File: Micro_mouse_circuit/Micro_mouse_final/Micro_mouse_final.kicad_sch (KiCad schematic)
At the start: 84 parts, among them J1 Conn_01x02, J2 USB_C_Receptacle_PowerOnly_6P, J3 Conn_02x16_Odd_Even, J4 Conn_01x01_Pin, U1 INA219AxDCN, U10 SN74LVC1G3157DCKR, U11 TPS22917DBVR, U12 AMS1117-3.3, U13 TPS22917DBVR, U14 SK22D15L5, U2 AMS1117-3.3, U3 HUSB237-AA001-DN06R, U4 MT3608, U5 LM2596SX-5_0/NOPB, U6 SK22D15L5, U7 L298N_C19922, U8 L298N_C19922, U9 TP4056_C382139

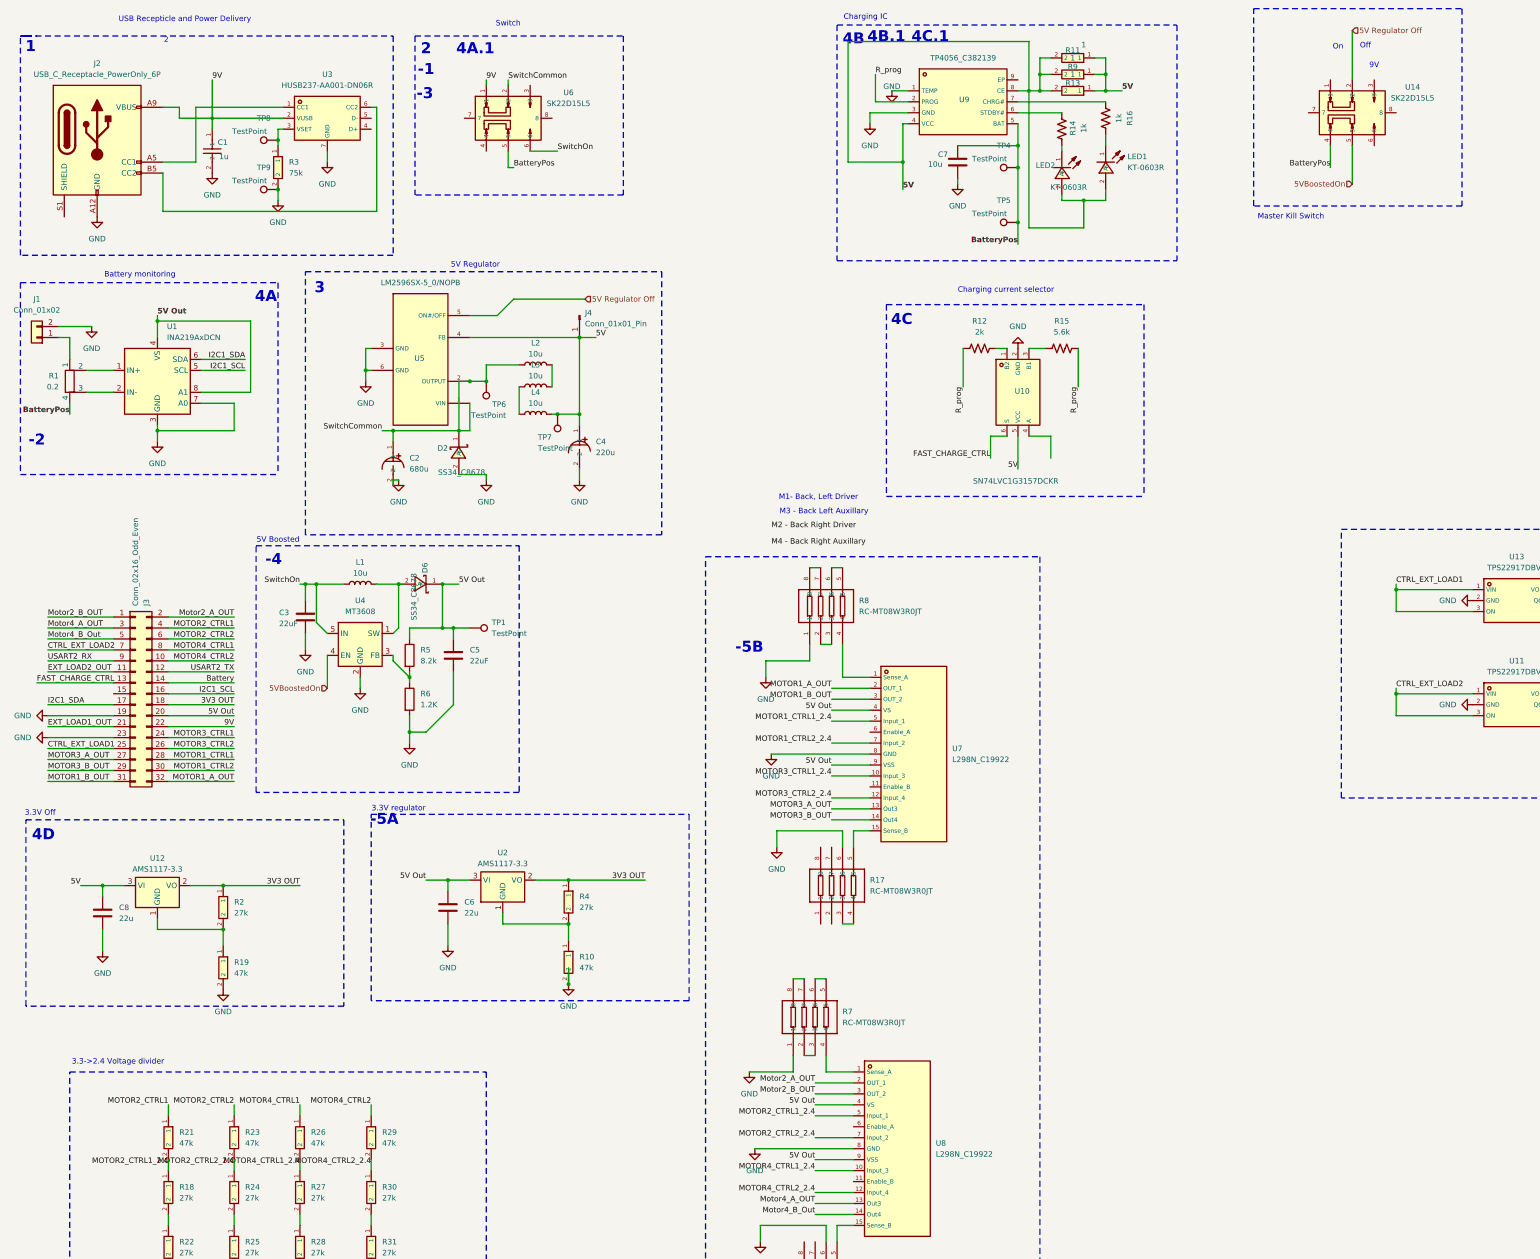
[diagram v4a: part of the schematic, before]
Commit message: push to Max - switch config finalized
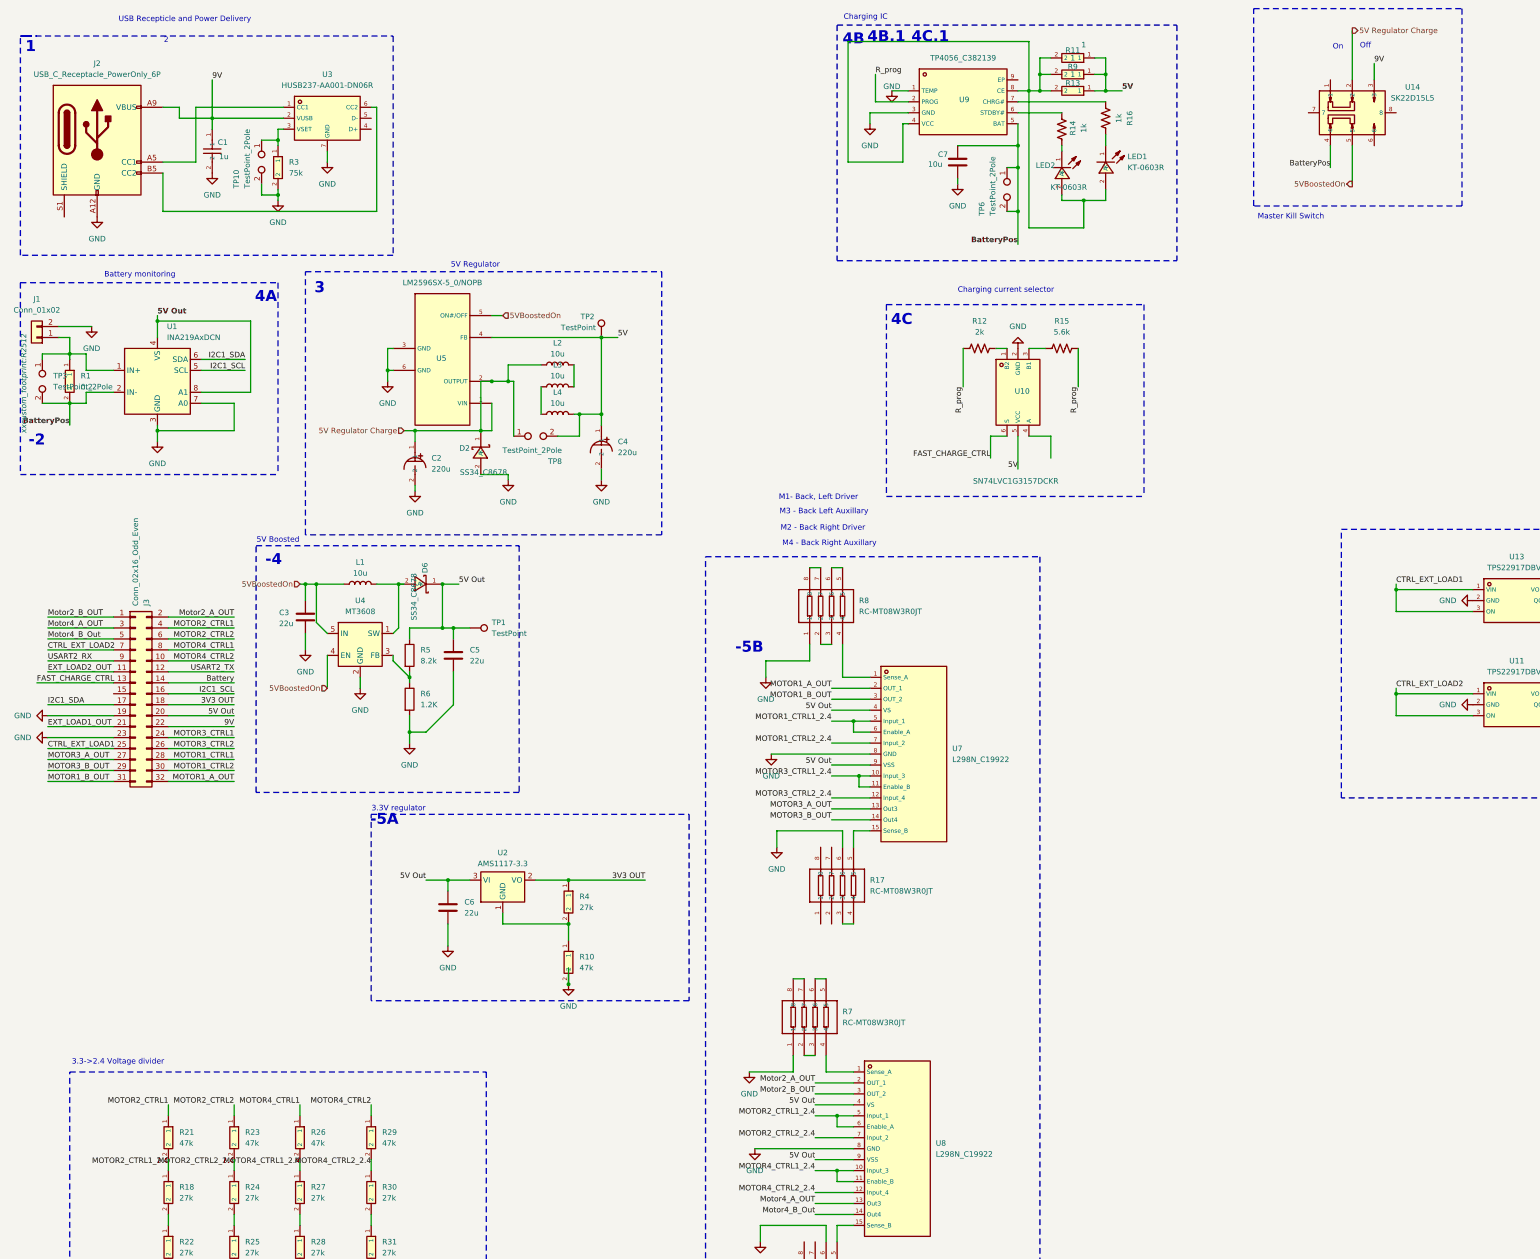
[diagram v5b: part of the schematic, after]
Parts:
- removed C2: 680u, xxcustom_footprint:CAP-TH_BD8.0-P3.50-D0.6-FD, symbol SPT1EM681F12OR:SPT1EM681F12OR
- removed C8: 22u, xxcustom_footprint:C1206, symbol Device:C
- removed J4: Conn_01x01_Pin, symbol Connector:Conn_01x01_Pin
- removed R1: 0.2, xxcustom_footprint:R2512, symbol Device:R_Shunt
- removed R19: 47k, xxcustom_footprint:R0805, symbol 0805W8F4702T5E:0805W8F4702T5E
- removed R2: 27k, xxcustom_footprint:R0805, symbol 0805W8F2702T5E:0805W8F2702T5E
- removed TP4, TP5, TP6, TP7, TP8, TP9: TestPoint, TestPoint:TestPoint_Pad_2.5x2.5mm, symbol Connector:TestPoint
- removed U12: AMS1117-3.3, Package_TO_SOT_SMD:SOT-223-3_TabPin2, symbol Regulator_Linear:AMS1117-3.3
- removed U6: SK22D15L5, xxcustom_footprint:SW-TH_XKB_SK22D15L7, symbol SK22D15L5:SK22D15L5
- added C2: 220u, xxcustom_footprint:CAP-SMD_BD6.3-L6.6-W6.6-FD, symbol RVT220UF10V67RV0037:RVT220UF10V67RV0037
- added R1: 0.2, xxcustom_footprint:R2512, symbol 0805W8F2702T5E:0805W8F2702T5E
- added TP10, TP3, TP6, TP8: TestPoint_2Pole, TestPoint:TestPoint_2Pads_Pitch2.54mm_Drill0.8mm, symbol Connector:TestPoint_2Pole
- added TP2: TestPoint, TestPoint:TestPoint_Pad_2.5x2.5mm, symbol Connector:TestPoint
- C3, C5: value 22uF -> 22u
- C7: LCSC (none) -> C7171
- J2: LCSC (none) -> C5187463
- L1, L2, L3, L4: LCSC (none) -> C1046
- LED2: LCSC C2286 -> C2290
- R12: LCSC (none) -> C17944
- R14, R16: LCSC (none) -> C4410
- R15: LCSC (none) -> C4382
- R17, R20, R7, R8: footprint XXmicromouse:RES-ARRAY-SMD_0402-8P-L2.0-W1.0-BL -> xxcustom_footprint:RES-ARRAY-SMD_0402-8P-L2.0-W1.0-BL
- R5: footprint XXmicromouse:R0805 -> xxcustom_footprint:R0805; LCSC (none) -> C17828
- R6: LCSC (none) -> C17379
- U1: LCSC (none) -> C87469
- U2: footprint XXmicromouse:SOT-223-3_L6.5-W3.4-P2.30-LS7.0-BR -> xxcustom_footprint:SOT-223-3_L6.5-W3.4-P2.30-LS7.0-BR; LCSC (none) -> C6186
- U4: LCSC (none) -> C84817
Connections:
- net SwitchCommon is gone; now on net 5V Regulator Charge: D2.1 (K), L2.1, U5.1 (VIN), U5.2 (OUTPUT)
- net SwitchOn is gone; now on net 5VBoostedOn: C3.1, L1.1, U4.5 (IN)
- net 5V: now also TP2.1, TP8.2; no longer LED1.2 (A), LED2.2 (A), R11.2, R13.2, R9.2, U9.4 (VCC), U9.8 (CE)
- net 5VBoostedOn: now also U5.5 (ON#/OFF)
- net 9V: now also U14.3
- net BatteryPos: now also U1.2 (IN-), R1.2, TP3.2, TP6.1, TP6.2
- net GND: now also C2.2, TP10.2
- net MOTOR1_CTRL1_2.4: now also U7.6 (Enable_A)
- net MOTOR2_CTRL1_2.4: now also U8.6 (Enable_A)
- net MOTOR3_CTRL1_2.4: now also U7.11 (Enable_B)
- net MOTOR4_CTRL1_2.4: now also U8.11 (Enable_B)
- net at R3.1, U3.3 (VSET): now also TP10.1
- net at U1.1 (IN+): now also J1.1 (Pin_1), R1.1, TP3.1
- net 5V Regulator Off renamed 5V Regulator Charge
- net 5V Regulator Charge: now also C2.1, TP8.1; no longer U5.5 (ON#/OFF)
- new net: LED1.2 (A), LED2.2 (A), R11.2, R13.2, R9.2, U9.4 (VCC), U9.8 (CE)
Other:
- note added: "M2 - Back Right Driver"
- note added: "M4 - Back Right Auxillary"
- note removed: "-1"
- note removed: "-3"
- note removed: "3.3V Off"
- note removed: "4A.1"
- note removed: "4D"
- note removed: "9V"
- note removed: "Switch"
- moved on the sheet: C4, D2, L2, L3, L4, U5

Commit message: common share update
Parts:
- removed TP2: TestPoint, TestPoint:TestPoint_Pad_2.5x2.5mm, symbol Connector:TestPoint
- removed U11, U13: TPS22917DBVR, xxcustom_footprint:SOT-23-6_L2.9-W1.6-P0.95-LS2.8-BR, symbol TPS22917DBVR:TPS22917DBVR
- added R19, R45: 75, xxcustom_footprint:R0603, symbol Device:R
- added R2, R44: 100, xxcustom_footprint:R0805, symbol Device:R
- added TP11, TP12, TP13, TP14, TP15, TP16, TP17, TP18, TP19, TP20: TestPoint, TestPoint:TestPoint_Pad_2.5x2.5mm, symbol Connector:TestPoint
- added TP4, TP5: TestPoint_2Pole, TestPoint:TestPoint_2Pads_Pitch2.54mm_Drill0.8mm, symbol Connector:TestPoint_2Pole
- added U12, U16: SS8550_C8542, Package_TO_SOT_SMD:SOT-23, symbol PNP - SS8550:SS8550_C8542
- added U15, U6: S9013_J3, Package_TO_SOT_SMD:SOT-23, symbol NPN - S9013:S9013_J3
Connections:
- net 5V Out is gone; now on net 5V: C5.1, C6.1, D6.1 (K), J3.20 (Pin_20), R5.1, TP1.1, U1.4 (VS), U1.8 (A1), U2.3 (VI), U7.4 (VS), U7.9 (VSS), U8.4 (VS), U8.9 (VSS)
- net Battery is gone; now on net BatteryPos: J3.14 (Pin_14)
- net 5V: now also R2.1, R44.1, TP5.1, U12.2 (E), U16.2 (E)
- net 5V Regulator Charge: now also TP4.1; no longer D2.1 (K), L2.1, TP8.1, U5.2 (OUTPUT)
- net CTRL_EXT_LOAD1: now also U6.1 (B)
- net CTRL_EXT_LOAD2: now also U15.1 (B)
- net EXT_LOAD1_OUT: now also TP19.1, U12.3 (C)
- net EXT_LOAD2_OUT: now also TP20.1, U16.3 (C)
- net GND: now also R19.2, R45.2, TP4.2, TP5.2
- net MOTOR1_CTRL1_2.4: now also TP17.1
- net MOTOR1_CTRL2_2.4: now also TP18.1
- net MOTOR2_CTRL1_2.4: now also TP11.1
- net MOTOR2_CTRL2_2.4: now also TP12.1
- net MOTOR3_CTRL1_2.4: now also TP15.1
- net MOTOR3_CTRL2_2.4: now also TP16.1
- net MOTOR4_CTRL1_2.4: now also TP13.1
- net MOTOR4_CTRL2_2.4: now also TP14.1
- new net: R2.2, U12.1 (B), U6.3 (C)
- new net: R45.1, U15.2 (E)
- new net: R44.2, U15.3 (C), U16.1 (B)
- new net: D2.1 (K), L2.1, TP8.1, U5.2 (OUTPUT)
- new net: R19.1, U6.2 (E)
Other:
- moved on the sheet: D2, R13, R25
